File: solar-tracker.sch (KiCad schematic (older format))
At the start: 5 parts, among them Q1 TIP41C, Q2 TIP41C, Q3 TIP42C, Q4 TIP42C, U1 LM324

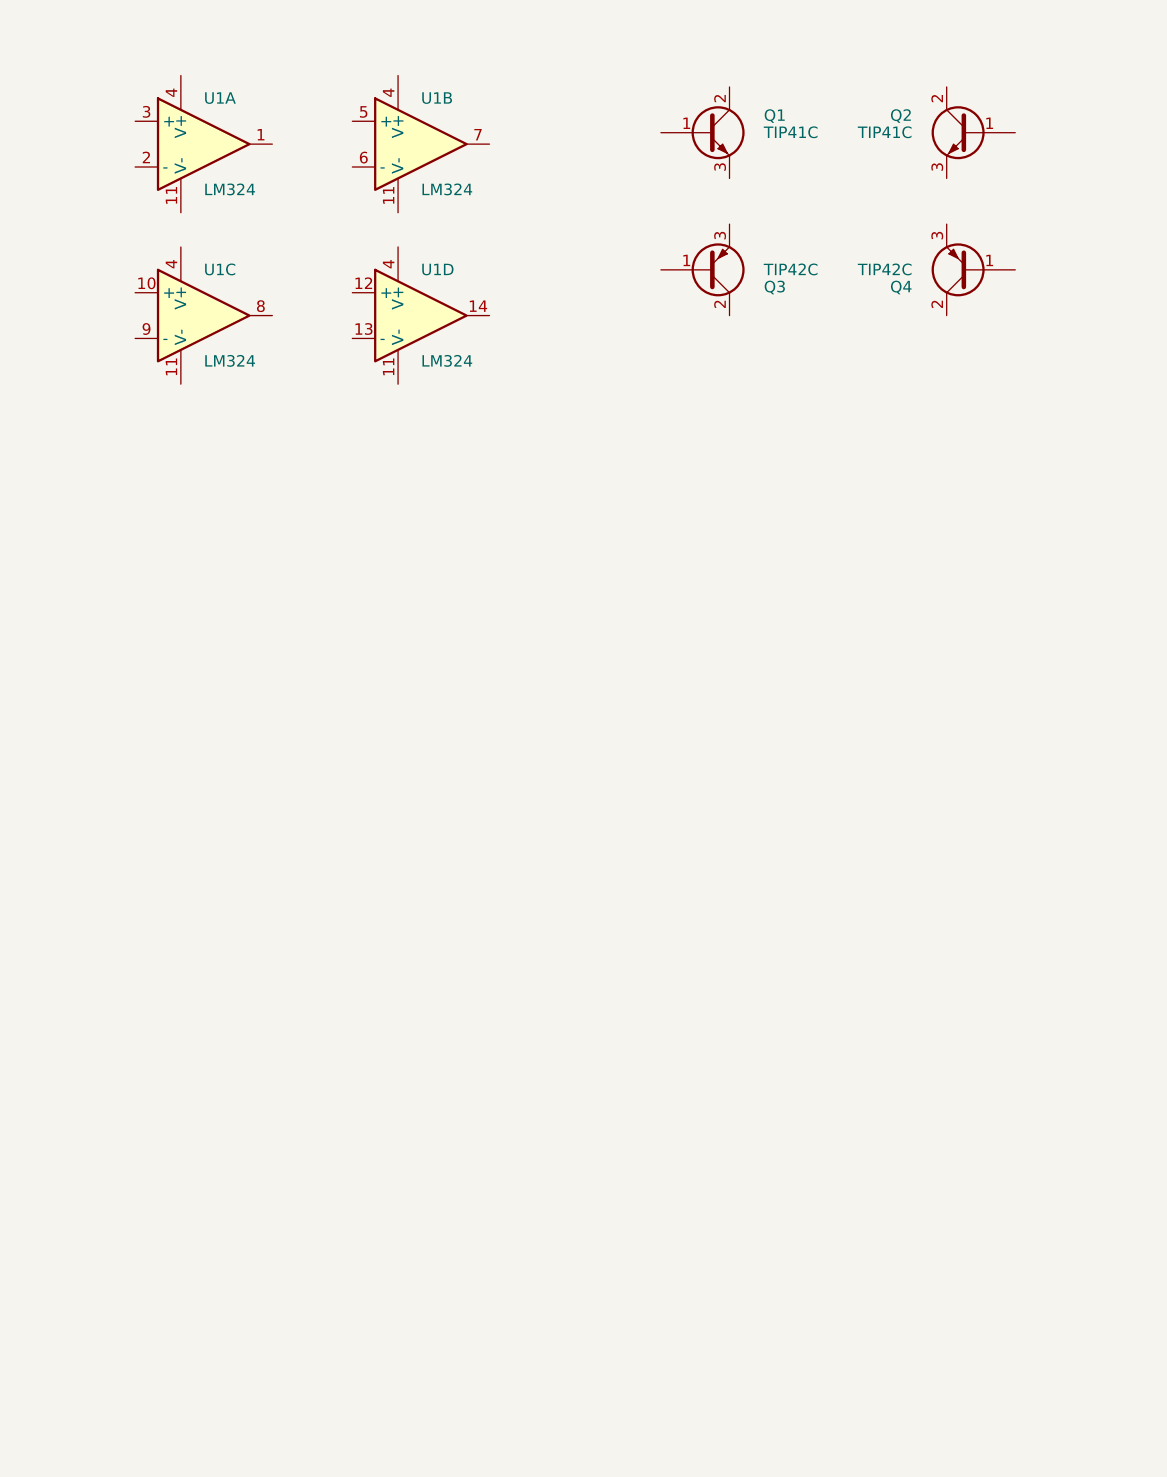
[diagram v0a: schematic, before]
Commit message: Started routing the PCB layout
Signed-off-by: Sam Protsenko <joe.skb7@gmail.com>
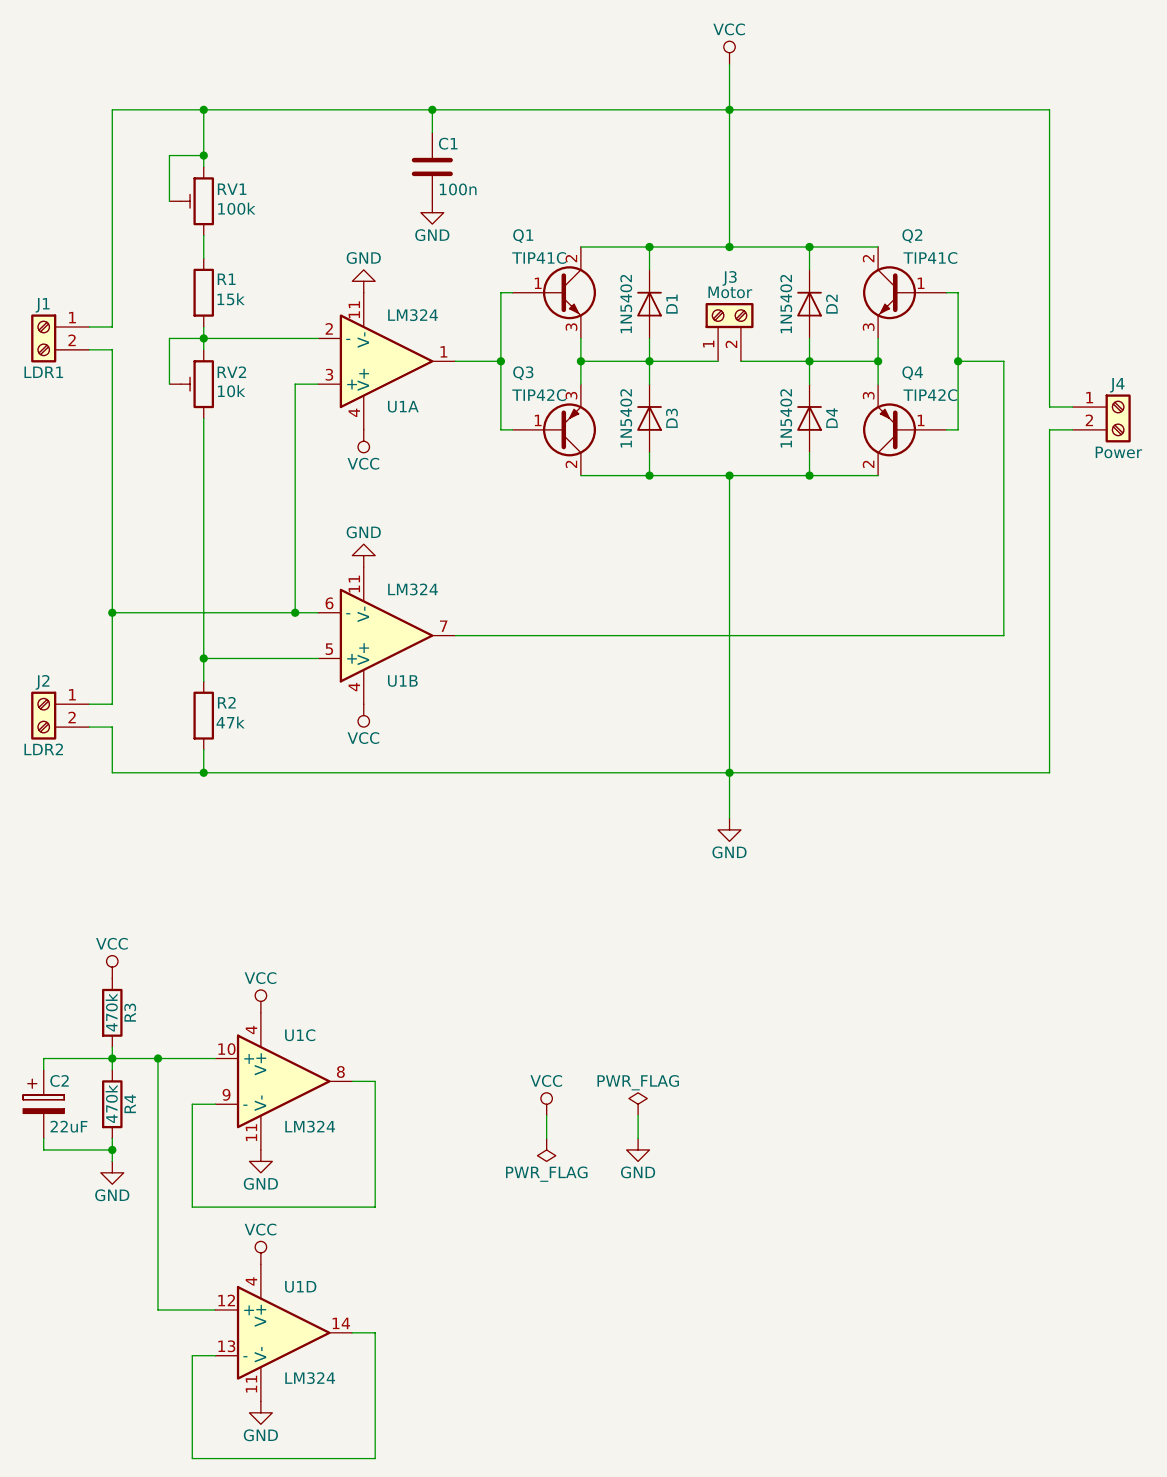
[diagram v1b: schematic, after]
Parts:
- added C1: 100n, Capacitors_THT:C_Disc_D5.0mm_W2.5mm_P5.00mm, symbol C
- added C2: 22uF, Capacitors_THT:CP_Radial_D8.0mm_P3.50mm, symbol CP
- added D1, D2, D3, D4: 1N5402, Diodes_THT:D_DO-201AD_P15.24mm_Horizontal, symbol 1N5402
- added J1: LDR1, Connectors_Terminal_Blocks:TerminalBlock_Pheonix_MKDS1.5-2pol, symbol Screw_Terminal_01x02
- added J2: LDR2, Connectors_Terminal_Blocks:TerminalBlock_Pheonix_MKDS1.5-2pol, symbol Screw_Terminal_01x02
- added J3: Motor, Connectors_Terminal_Blocks:TerminalBlock_Pheonix_MKDS1.5-2pol, symbol Screw_Terminal_01x02
- added J4: Power, Connectors_Terminal_Blocks:TerminalBlock_Pheonix_MKDS1.5-2pol, symbol Screw_Terminal_01x02
- added R1: 15k, Resistors_THT:R_Axial_DIN0207_L6.3mm_D2.5mm_P10.16mm_Horizontal, symbol R
- added R2: 47k, Resistors_THT:R_Axial_DIN0207_L6.3mm_D2.5mm_P10.16mm_Horizontal, symbol R
- added R3, R4: 470k, Resistors_THT:R_Axial_DIN0207_L6.3mm_D2.5mm_P10.16mm_Horizontal, symbol R
- added RV1: 100k, Potentiometers:Potentiometer_Trimmer_Bourns_3266W, symbol POT_TRIM
- added RV2: 10k, Potentiometers:Potentiometer_Trimmer_Bourns_3266W, symbol POT_TRIM
- U1: footprint (none) -> Housings_DIP:DIP-14_W7.62mm
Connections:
- net at U1.1: now also Q1.1 (B), Q3.1 (B)
- net GND: now reaches U1.11 (V-)
- net GND: now also Q3.2 (C), Q4.2 (C), U1.11 (V-), U1.11 (V-), U1.11 (V-), C1.2, C2.2, D3.2 (A), D4.2 (A), J2.2 (Pin_2), J4.2 (Pin_2), R2.2, R4.2
- net at U1.2 (-): now also R1.2, RV2.1, RV2.2
- net at U1.3 (+): now also U1.6 (-), J1.2 (Pin_2), J2.1 (Pin_1)
- net VCC: now reaches U1.4 (V+)
- net VCC: now also Q1.2 (C), Q2.2 (C), U1.4 (V+), U1.4 (V+), U1.4 (V+), C1.1, D1.1 (K), D2.1 (K), J1.1 (Pin_1), J4.1 (Pin_1), R3.1, RV1.1, RV1.2
- net at U1.5 (+): now also R2.1, RV2.3
- net at U1.7: now also Q2.1 (B), Q4.1 (B)
- net at U1.10 (+): now also U1.12 (+), C2.1, R3.2, R4.1
- net at U1.8: now also U1.9 (-)
- net at U1.13 (-): now also U1.14
- net at Q1.3 (E): now also Q3.3 (E), D1.2 (A), D3.1 (K), J3.1 (Pin_1)
- net at Q2.3 (E): now also Q4.3 (E), D2.2 (A), D4.1 (K), J3.2 (Pin_2)
- new net: R1.1, RV1.3
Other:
- moved on the sheet: Q1, Q2, Q3, Q4, U1A, U1B, U1C, U1D

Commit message: Create PCB layout for blocks
Signed-off-by: Sam Protsenko <joe.skb7@gmail.com>
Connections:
- net GND: now also J4.1 (Pin_1); no longer J4.2 (Pin_2)
- net VCC: now also J4.2 (Pin_2); no longer J4.1 (Pin_1)
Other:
- moved on the sheet: J4
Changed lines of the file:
@@
 $EndComp
 $Comp
-L GND #PWR01
+L GND #PWR9
 U 1 1 5A191833
 P 2200 3000
-F 0 "#PWR01" H 2200 2750 50  0001 C CNN
+F 0 "#PWR9" H 2200 2750 50  0001 C CNN
 F 1 "GND" H 2200 2850 50  0000 C CNN
 F 2 "" H 2200 3000 50  0001 C CNN
@@
 $EndComp
 $Comp
-L GND #PWR02
+L GND #PWR4
 U 1 1 5A19198A
 P 1750 5550
-F 0 "#PWR02" H 1750 5300 50  0001 C CNN
+F 0 "#PWR4" H 1750 5300 50  0001 C CNN
 F 1 "GND" H 1750 5400 50  0000 C CNN
 F 2 "" H 1750 5550 50  0001 C CNN
@@
 $EndComp
 $Comp
-L VCC #PWR03
+L VCC #PWR10
 U 1 1 5A1928D2
 P 2200 3600
-F 0 "#PWR03" H 2200 3450 50  0001 C CNN
+F 0 "#PWR10" H 2200 3450 50  0001 C CNN
 F 1 "VCC" H 2200 3750 50  0000 C CNN
 F 2 "" H 2200 3600 50  0001 C CNN
@@
 $EndComp
 $Comp
-L VCC #PWR04
+L VCC #PWR3
 U 1 1 5A1929F0
 P 1750 4950
-F 0 "#PWR04" H 1750 4800 50  0001 C CNN
+F 0 "#PWR3" H 1750 4800 50  0001 C CNN
 F 1 "VCC" H 1750 5100 50  0000 C CNN
 F 2 "" H 1750 4950 50  0001 C CNN
@@
 $EndComp
 $Comp
-L VCC #PWR05
+L VCC #PWR1
 U 1 1 5A19362A
 P 1100 4800
-F 0 "#PWR05" H 1100 4650 50  0001 C CNN
+F 0 "#PWR1" H 1100 4650 50  0001 C CNN
 F 1 "VCC" H 1100 4950 50  0000 C CNN
 F 2 "" H 1100 4800 50  0001 C CNN
@@
 $EndComp
 $Comp
-L GND #PWR06
+L GND #PWR2
 U 1 1 5A19367D
 P 1100 5600
-F 0 "#PWR06" H 1100 5350 50  0001 C CNN
+F 0 "#PWR2" H 1100 5350 50  0001 C CNN
 F 1 "GND" H 1100 5450 50  0000 C CNN
 F 2 "" H 1100 5600 50  0001 C CNN
@@
 $EndComp
 $Comp
-L VCC #PWR07
+L VCC #PWR14
 U 1 1 5A198F5C
 P 3800 800
-F 0 "#PWR07" H 3800 650 50  0001 C CNN
+F 0 "#PWR14" H 3800 650 50  0001 C CNN
 F 1 "VCC" H 3800 950 50  0000 C CNN
 F 2 "" H 3800 800 50  0001 C CNN
@@
 $EndComp
 $Comp
-L GND #PWR08
+L GND #PWR15
 U 1 1 5A199159
 P 3800 4100
-F 0 "#PWR08" H 3800 3850 50  0001 C CNN
+F 0 "#PWR15" H 3800 3850 50  0001 C CNN
 F 1 "GND" H 3800 3950 50  0000 C CNN
 F 2 "" H 3800 4100 50  0001 C CNN
@@
 F 3 "" H 5500 2300 50  0001 C CNN
 	1    5500 2300
-	1    0    0    -1
+	1    0    0    1
 $EndComp
 $Comp
@@
 	1100 1000 5200 1000
 Wire Wire Line
-	5300 2300 5200 2300
-Wire Wire Line
-	5200 2300 5200 1000
-Wire Wire Line
-	5300 2400 5200 2400
-Wire Wire Line
-	5200 2400 5200 3900
-Wire Wire Line
 	2500 1100 2500 1000
 Connection ~ 2500 1000
 $Comp
-L GND #PWR09
+L GND #PWR11
 U 1 1 5A19D40A
 P 2500 1400
-F 0 "#PWR09" H 2500 1150 50  0001 C CNN
+F 0 "#PWR11" H 2500 1150 50  0001 C CNN
 F 1 "GND" H 2500 1250 50  0000 C CNN
 F 2 "" H 2500 1400 50  0001 C CNN
@@
 $EndComp
 $Comp
-L VCC #PWR010
+L VCC #PWR8
 U 1 1 5A192872
 P 2200 2400
-F 0 "#PWR010" H 2200 2250 50  0001 C CNN
+F 0 "#PWR8" H 2200 2250 50  0001 C CNN
 F 1 "VCC" H 2200 2550 50  0000 C CNN
 F 2 "" H 2200 2400 50  0001 C CNN
@@
 $EndComp
 $Comp
-L GND #PWR011
+L GND #PWR7
 U 1 1 5A190031
 P 2200 1800
-F 0 "#PWR011" H 2200 1550 50  0001 C CNN
+F 0 "#PWR7" H 2200 1550 50  0001 C CNN
 F 1 "GND" H 2200 1650 50  0000 C CNN
 F 2 "" H 2200 1800 50  0001 C CNN
@@
 $EndComp
 $Comp
-L GND #PWR012
+L GND #PWR6
 U 1 1 5A191B79
 P 1750 6650
-F 0 "#PWR012" H 1750 6400 50  0001 C CNN
+F 0 "#PWR6" H 1750 6400 50  0001 C CNN
 F 1 "GND" H 1750 6500 50  0000 C CNN
 F 2 "" H 1750 6650 50  0001 C CNN
@@
 $EndComp
 $Comp
-L VCC #PWR013
+L VCC #PWR5
 U 1 1 5A192B0E
 P 1750 6050
-F 0 "#PWR013" H 1750 5900 50  0001 C CNN
+F 0 "#PWR5" H 1750 5900 50  0001 C CNN
 F 1 "VCC" H 1750 6200 50  0000 C CNN
 F 2 "" H 1750 6050 50  0001 C CNN
@@
 $EndComp
 $Comp
-L PWR_FLAG #FLG014
+L PWR_FLAG #FLG1
 U 1 1 5A1A06D6
 P 3000 5500
-F 0 "#FLG014" H 3000 5575 50  0001 C CNN
+F 0 "#FLG1" H 3000 5575 50  0001 C CNN
 F 1 "PWR_FLAG" H 3000 5650 50  0000 C CNN
 F 2 "" H 3000 5500 50  0001 C CNN
@@
 $EndComp
 $Comp
-L VCC #PWR015
+L VCC #PWR12
 U 1 1 5A1A07C2
 P 3000 5400
-F 0 "#PWR015" H 3000 5250 50  0001 C CNN
+F 0 "#PWR12" H 3000 5250 50  0001 C CNN
 F 1 "VCC" H 3000 5550 50  0000 C CNN
 F 2 "" H 3000 5400 50  0001 C CNN
@@
 $EndComp
 $Comp
-L GND #PWR016
+L GND #PWR13
 U 1 1 5A1A091E
 P 3400 5500
-F 0 "#PWR016" H 3400 5250 50  0001 C CNN
+F 0 "#PWR13" H 3400 5250 50  0001 C CNN
 F 1 "GND" H 3400 5350 50  0000 C CNN
 F 2 "" H 3400 5500 50  0001 C CNN
@@
 $EndComp
 $Comp
-L PWR_FLAG #FLG017
+L PWR_FLAG #FLG2
 U 1 1 5A1A0992
 P 3400 5400
-F 0 "#FLG017" H 3400 5475 50  0001 C CNN
+F 0 "#FLG2" H 3400 5475 50  0001 C CNN
 F 1 "PWR_FLAG" H 3400 5550 50  0000 C CNN
 F 2 "" H 3400 5400 50  0001 C CNN
@@
 Wire Wire Line
 	3400 5400 3400 5500
+Wire Wire Line
+	5300 2200 5200 2200
+Wire Wire Line
+	5200 2200 5200 1000
+Wire Wire Line
+	5300 2300 5200 2300
+Wire Wire Line
+	5200 2300 5200 3900
 $EndSCHEMATC
